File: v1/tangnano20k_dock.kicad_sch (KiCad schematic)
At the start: 42 parts, among them J1 Mini-DIN-6, J2 2x20 Pin Female, J3 Conn_01x03_Male, J4 Conn_01x20, J5 Conn_01x02, J6 RCA, J7 FCR684205T, J8 AudioJack3, U1 TXS0104E, U2 TangNano20K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

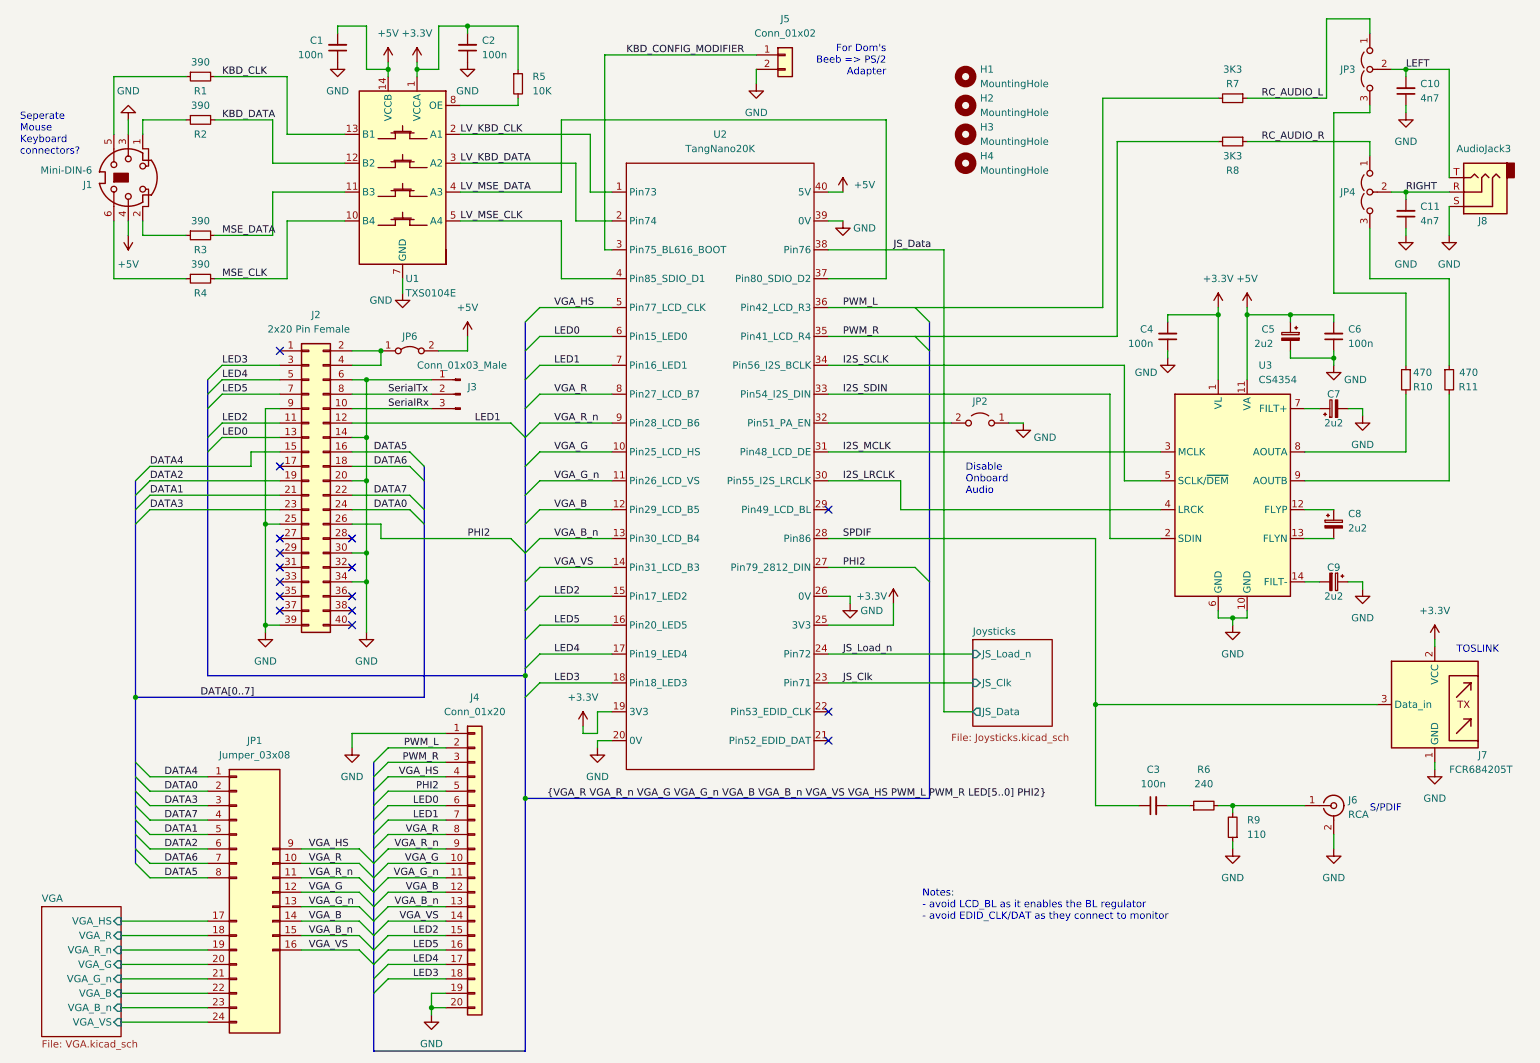
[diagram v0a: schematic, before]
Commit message: Add KEY_CONF to DEBUG header
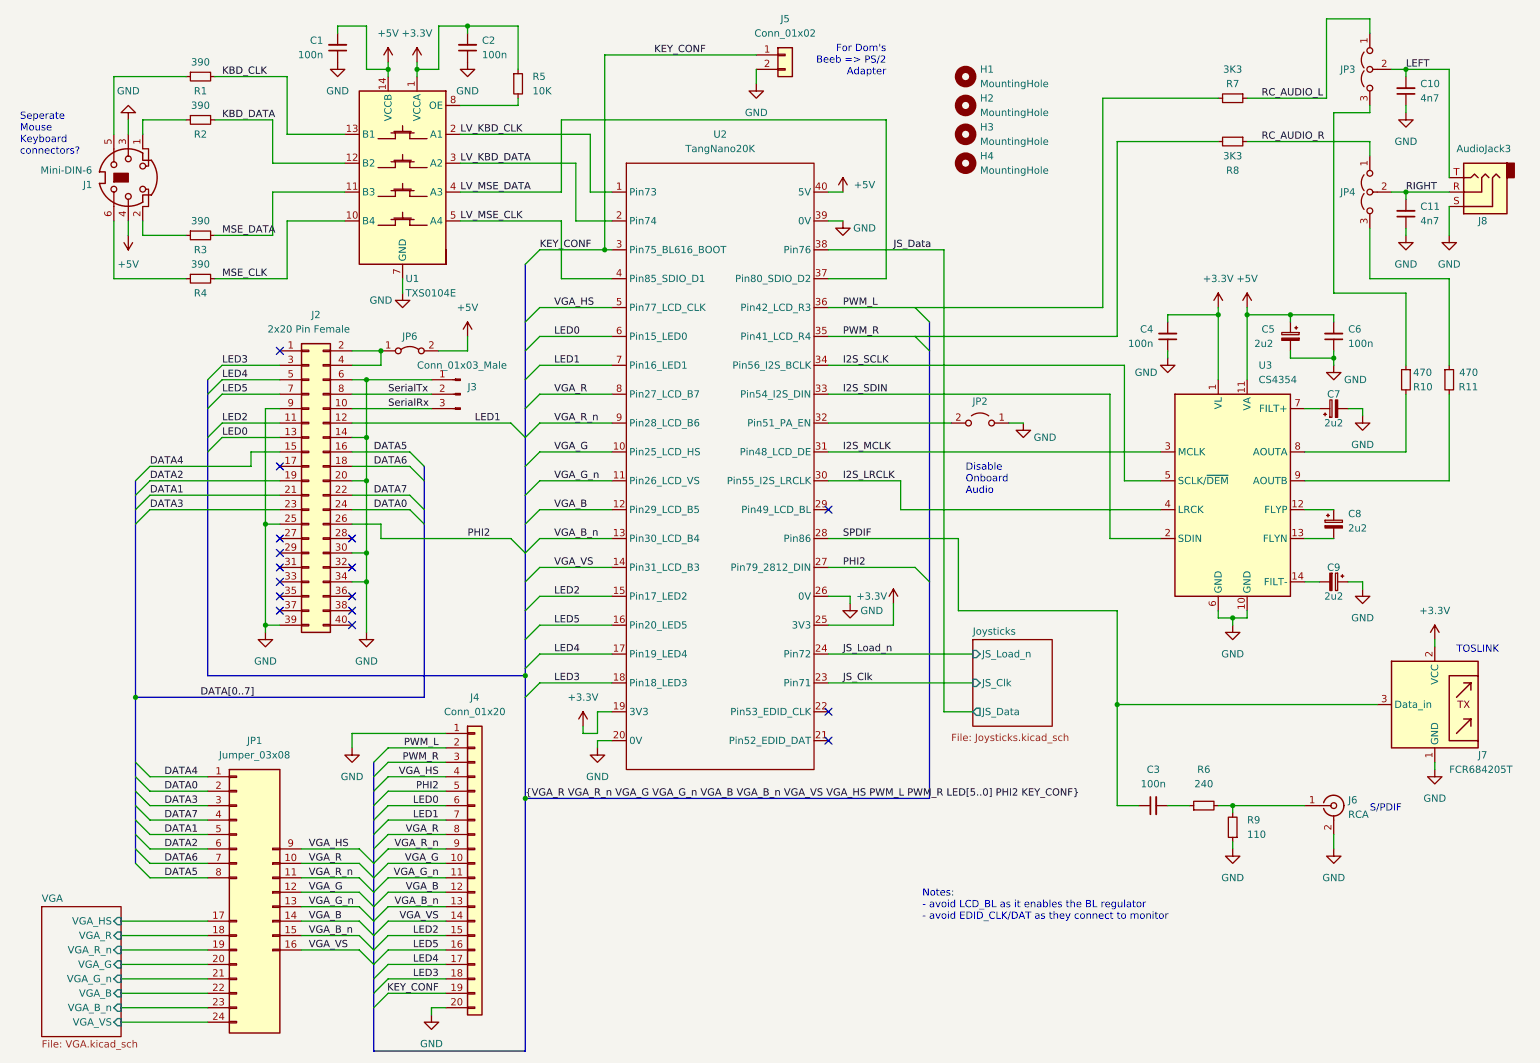
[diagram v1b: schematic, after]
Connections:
- net GND: no longer J4.19 (Pin_19)
- net KBD_CONFIG_MODIFIER renamed KEY_CONF
- net KEY_CONF: now also J4.19 (Pin_19)
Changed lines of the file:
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@@
   (junction (at 80.01 87.63) (diameter 0) (color 0 0 0 0)
   )
-  (junction (at 208.28 134.62) (diameter 0) (color 0 0 0 0)
-  )
   (junction (at 80.01 77.47) (diameter 0) (color 0 0 0 0)
   )
   (junction (at 62.23 102.87) (diameter 0) (color 0 0 0 0)
   )
-  (junction (at 91.44 187.96) (diameter 0) (color 0 0 0 0)
-  )
   (junction (at 39.37 133.35) (diameter 0) (color 0 0 0 0)
   )
@@
   (junction (at 62.23 120.65) (diameter 0) (color 0 0 0 0)
   )
+  (junction (at 212.09 134.62) (diameter 0) (color 0 0 0 0)
+  )
   (junction (at 82.55 72.39) (diameter 0) (color 0 0 0 0)
   )
@@
   (junction (at 242.57 66.04) (diameter 0) (color 0 0 0 0)
   )
+  (junction (at 121.92 54.61) (diameter 0) (color 0 0 0 0)
+  )
   (junction (at 80.01 95.25) (diameter 0) (color 0 0 0 0)
   )
@@
     (stroke (width 0) (type default) (color 0 0 0 0))
   )
+  (bus_entry (at 83.82 185.42) (size -2.54 2.54)
+    (stroke (width 0) (type default) (color 0 0 0 0))
+  )
   (bus_entry (at 41.91 154.94) (size -2.54 -2.54)
     (stroke (width 0) (type default) (color 0 0 0 0))
@@
     (stroke (width 0) (type default) (color 0 0 0 0))
   )
+  (bus_entry (at 110.49 54.61) (size -2.54 2.54)
+    (stroke (width 0) (type default) (color 0 0 0 0))
+  )
   (bus_entry (at 54.61 85.09) (size -2.54 2.54)
     (stroke (width 0) (type default) (color 0 0 0 0))
@@
     (stroke (width 0) (type default) (color 0 0 0 0))
   )
+  (wire (pts (xy 110.49 54.61) (xy 121.92 54.61))
+    (stroke (width 0) (type default) (color 0 0 0 0))
+  )
   (wire (pts (xy 212.09 35.56) (xy 229.87 35.56))
     (stroke (width 0) (type default) (color 0 0 0 0))
@@
     (stroke (width 0) (type default) (color 0 0 0 0))
   )
+  (wire (pts (xy 212.09 134.62) (xy 257.81 134.62))
+    (stroke (width 0) (type default) (color 0 0 0 0))
+  )
   (wire (pts (xy 40.64 31.75) (xy 48.26 31.75))
     (stroke (width 0) (type default) (color 0 0 0 0))
@@
     (stroke (width 0) (type default) (color 0 0 0 0))
   )
+  (wire (pts (xy 93.98 185.42) (xy 83.82 185.42))
+    (stroke (width 0) (type default) (color 0 0 0 0))
+  )
   (wire (pts (xy 53.34 59.69) (xy 66.04 59.69))
     (stroke (width 0) (type default) (color 0 0 0 0))
@@
     (stroke (width 0) (type default) (color 0 0 0 0))
   )
-  (wire (pts (xy 91.44 187.96) (xy 91.44 185.42))
-    (stroke (width 0) (type default) (color 0 0 0 0))
-  )
   (bus (pts (xy 81.28 144.78) (xy 81.28 147.32))
     (stroke (width 0) (type default) (color 0 0 0 0))
@@
     (stroke (width 0) (type default) (color 0 0 0 0))
   )
+  (wire (pts (xy 212.09 118.11) (xy 212.09 134.62))
+    (stroke (width 0) (type default) (color 0 0 0 0))
+  )
   (bus (pts (xy 107.95 77.47) (xy 107.95 82.55))
     (stroke (width 0) (type default) (color 0 0 0 0))
@@
     (stroke (width 0) (type default) (color 0 0 0 0))
   )
-  (wire (pts (xy 161.29 105.41) (xy 208.28 105.41))
+  (wire (pts (xy 161.29 105.41) (xy 184.15 105.41))
     (stroke (width 0) (type default) (color 0 0 0 0))
   )
@@
     (stroke (width 0) (type default) (color 0 0 0 0))
   )
-  (wire (pts (xy 208.28 134.62) (xy 257.81 134.62))
-    (stroke (width 0) (type default) (color 0 0 0 0))
-  )
   (wire (pts (xy 110.49 74.93) (xy 123.19 74.93))
     (stroke (width 0) (type default) (color 0 0 0 0))
@@
     (stroke (width 0) (type default) (color 0 0 0 0))
   )
-  (wire (pts (xy 208.28 105.41) (xy 208.28 134.62))
-    (stroke (width 0) (type default) (color 0 0 0 0))
-  )
   (wire (pts (xy 106.68 29.21) (xy 106.68 27.94))
     (stroke (width 0) (type default) (color 0 0 0 0))
@@
     (stroke (width 0) (type default) (color 0 0 0 0))
   )
-  (wire (pts (xy 208.28 152.4) (xy 215.9 152.4))
+  (wire (pts (xy 212.09 152.4) (xy 215.9 152.4))
     (stroke (width 0) (type default) (color 0 0 0 0))
   )
@@
     (stroke (width 0) (type default) (color 0 0 0 0))
   )
+  (wire (pts (xy 184.15 118.11) (xy 212.09 118.11))
+    (stroke (width 0) (type default) (color 0 0 0 0))
+  )
   (wire (pts (xy 232.41 158.75) (xy 232.41 160.02))
     (stroke (width 0) (type default) (color 0 0 0 0))
@@
     (stroke (width 0) (type default) (color 0 0 0 0))
   )
+  (wire (pts (xy 184.15 105.41) (xy 184.15 118.11))
+    (stroke (width 0) (type default) (color 0 0 0 0))
+  )
   (bus (pts (xy 107.95 133.35) (xy 107.95 151.13))
     (stroke (width 0) (type default) (color 0 0 0 0))
@@
     (stroke (width 0) (type default) (color 0 0 0 0))
   )
-  (wire (pts (xy 208.28 134.62) (xy 208.28 152.4))
+  (wire (pts (xy 212.09 134.62) (xy 212.09 152.4))
     (stroke (width 0) (type default) (color 0 0 0 0))
   )
@@
     (stroke (width 0) (type default) (color 0 0 0 0))
   )
-  (wire (pts (xy 91.44 185.42) (xy 93.98 185.42))
-    (stroke (width 0) (type default) (color 0 0 0 0))
-  )
   (wire (pts (xy 36.83 172.72) (xy 52.07 172.72))
     (stroke (width 0) (type default) (color 0 0 0 0))
@@
     (stroke (width 0) (type default) (color 0 0 0 0))
   )
-  (bus (pts (xy 81.28 185.42) (xy 81.28 195.58))
+  (bus (pts (xy 81.28 185.42) (xy 81.28 187.96))
     (stroke (width 0) (type default) (color 0 0 0 0))
   )
@@
     (stroke (width 0) (type default) (color 0 0 0 0))
   )
+  (bus (pts (xy 81.28 187.96) (xy 81.28 195.58))
+    (stroke (width 0) (type default) (color 0 0 0 0))
+  )
   (wire (pts (xy 62.23 82.55) (xy 62.23 102.87))
     (stroke (width 0) (type default) (color 0 0 0 0))
@@
     (stroke (width 0) (type default) (color 0 0 0 0))
   )
+  (bus (pts (xy 107.95 57.15) (xy 107.95 67.31))
+    (stroke (width 0) (type default) (color 0 0 0 0))
+  )
   (wire (pts (xy 68.58 175.26) (xy 78.74 175.26))
     (stroke (width 0) (type default) (color 0 0 0 0))
@@
     (effects (font (size 1.27 1.27)) (justify right bottom))
   )
-  (label "{VGA_R VGA_R_n VGA_G VGA_G_n VGA_B VGA_B_n VGA_VS VGA_HS PWM_L PWM_R LED[5..0] PHI2}"
-    (at 111.76 151.13 0)
+  (label "{VGA_R VGA_R_n VGA_G VGA_G_n VGA_B VGA_B_n VGA_VS VGA_HS PWM_L PWM_R LED[5..0] PHI2 KEY_CONF}"
+    (at 107.95 151.13 0)
     (effects (font (size 1.27 1.27)) (justify left bottom))
   )
@@
     (effects (font (size 1.27 1.27)) (justify left bottom))
   )
+  (label "KEY_CONF" (at 92.71 185.42 180)
+    (effects (font (size 1.27 1.27)) (justify right bottom))
+  )
   (label "RC_AUDIO_R" (at 237.49 35.56 0)
     (effects (font (size 1.27 1.27)) (justify left bottom))
@@
     (effects (font (size 1.27 1.27)) (justify right bottom))
   )
-  (label "KBD_CONFIG_MODIFIER" (at 125.73 20.32 0)
-    (effects (font (size 1.27 1.27)) (justify left bottom))
+  (label "KEY_CONF" (at 139.7 20.32 180)
+    (effects (font (size 1.27 1.27)) (justify right bottom))
   )
   (label "PHI2" (at 97.79 105.41 0)
@@
     (effects (font (size 1.27 1.27)) (justify right bottom))
   )
+  (label "KEY_CONF" (at 110.49 54.61 0)
+    (effects (font (size 1.27 1.27)) (justify left bottom))
+  )
   (label "DATA[0..7]" (at 50.8 133.35 0)

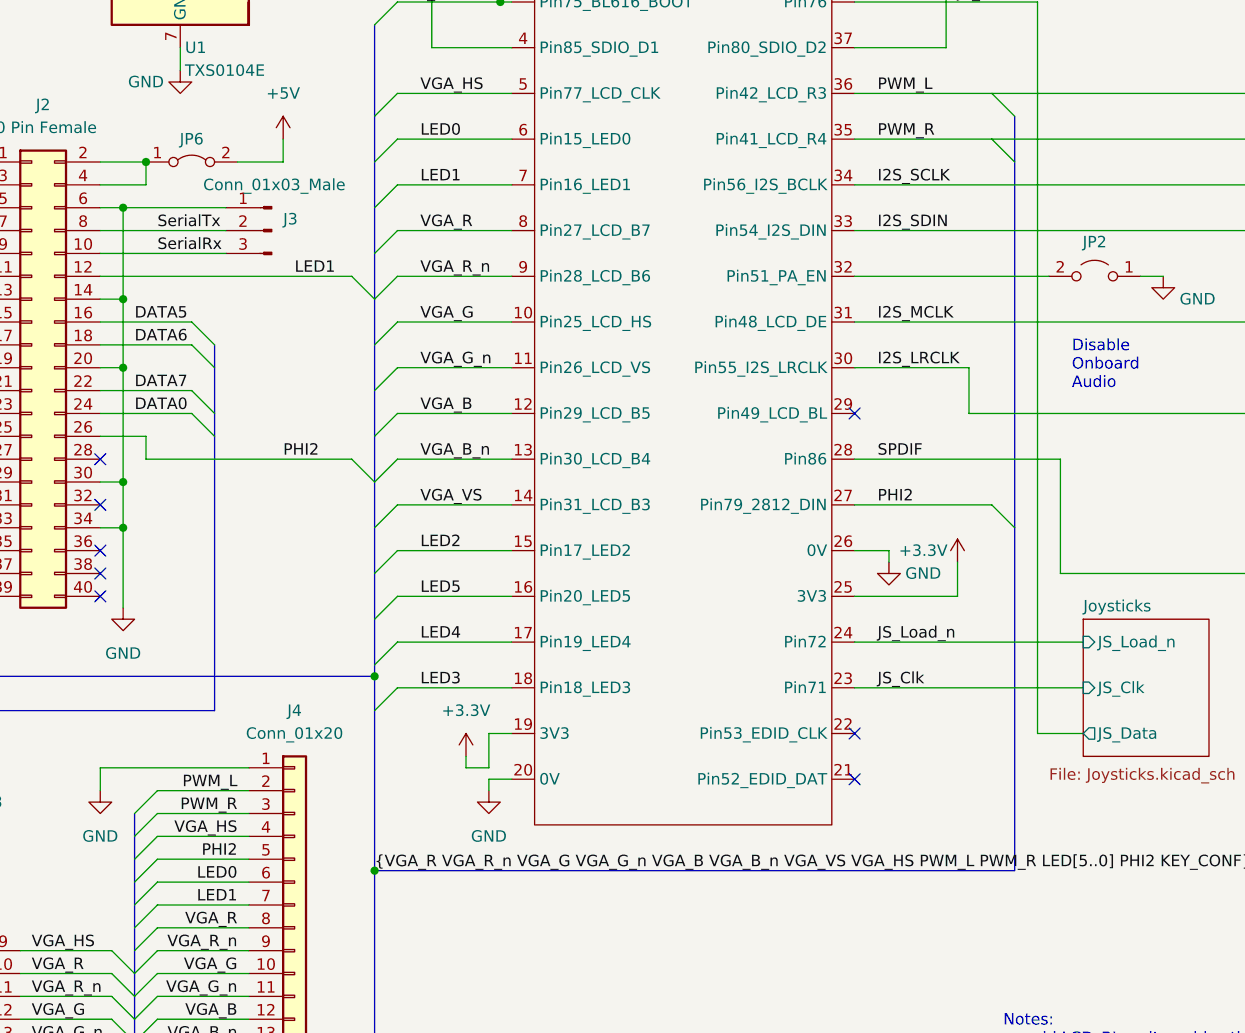
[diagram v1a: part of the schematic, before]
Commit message: Drive PiTube PHI2 from js_clk to save a pin
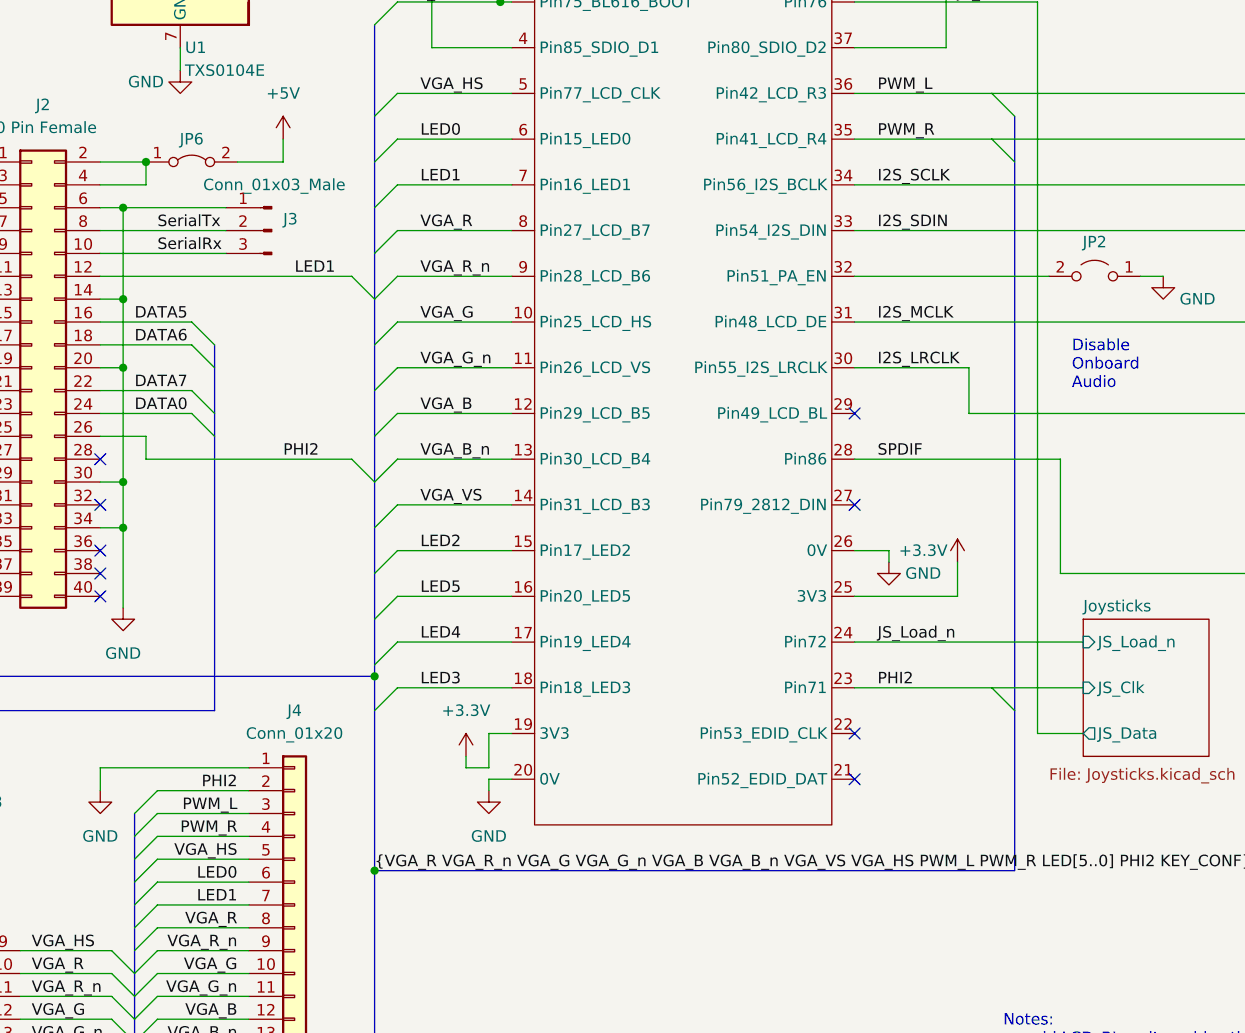
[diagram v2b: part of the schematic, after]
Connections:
- net JS_Clk is gone; now on net PHI2: U2.23 (Pin71)
- net PHI2: now also J4.2 (Pin_2); no longer J4.5 (Pin_5), U2.27 (Pin79_2812_DIN)
- net PWM_L: now also J4.3 (Pin_3); no longer J4.2 (Pin_2)
- net PWM_R: now also J4.4 (Pin_4); no longer J4.3 (Pin_3)
- net VGA_HS: now also J4.5 (Pin_5); no longer J4.4 (Pin_4)
- no-connect marks 16 -> 17
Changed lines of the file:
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@@
   (no_connect (at 64.77 107.95))
   (no_connect (at 64.77 72.39))
+  (no_connect (at 161.29 110.49))
   (no_connect (at 161.29 135.89))
   (no_connect (at 161.29 100.33))
@@
     (stroke (width 0) (type default) (color 0 0 0 0))
   )
-  (bus_entry (at 176.53 110.49) (size 2.54 2.54)
+  (bus_entry (at 176.53 130.81) (size 2.54 2.54)
     (stroke (width 0) (type default) (color 0 0 0 0))
   )
@@
     (stroke (width 0) (type default) (color 0 0 0 0))
   )
-  (bus (pts (xy 179.07 72.39) (xy 179.07 113.03))
-    (stroke (width 0) (type default) (color 0 0 0 0))
-  )
   (wire (pts (xy 74.93 15.24) (xy 80.01 15.24))
     (stroke (width 0) (type default) (color 0 0 0 0))
@@
     (stroke (width 0) (type default) (color 0 0 0 0))
   )
-  (wire (pts (xy 161.29 110.49) (xy 176.53 110.49))
-    (stroke (width 0) (type default) (color 0 0 0 0))
-  )
   (wire (pts (xy 36.83 185.42) (xy 52.07 185.42))
     (stroke (width 0) (type default) (color 0 0 0 0))
@@
     (stroke (width 0) (type default) (color 0 0 0 0))
   )
+  (bus (pts (xy 179.07 133.35) (xy 179.07 151.13))
+    (stroke (width 0) (type default) (color 0 0 0 0))
+  )
   (bus (pts (xy 81.28 157.48) (xy 81.28 160.02))
     (stroke (width 0) (type default) (color 0 0 0 0))
@@
     (stroke (width 0) (type default) (color 0 0 0 0))
   )
-  (wire (pts (xy 161.29 130.81) (xy 186.69 130.81))
+  (wire (pts (xy 161.29 130.81) (xy 176.53 130.81))
     (stroke (width 0) (type default) (color 0 0 0 0))
   )
@@
     (stroke (width 0) (type default) (color 0 0 0 0))
   )
+  (wire (pts (xy 176.53 130.81) (xy 186.69 130.81))
+    (stroke (width 0) (type default) (color 0 0 0 0))
+  )
   (bus (pts (xy 107.95 87.63) (xy 107.95 92.71))
     (stroke (width 0) (type default) (color 0 0 0 0))
@@
     (stroke (width 0) (type default) (color 0 0 0 0))
   )
-  (bus (pts (xy 179.07 113.03) (xy 179.07 151.13))
+  (bus (pts (xy 179.07 72.39) (xy 179.07 133.35))
     (stroke (width 0) (type default) (color 0 0 0 0))
   )
@@
     (effects (font (size 1.27 1.27)) (justify left bottom))
   )
-  (label "PWM_R" (at 92.71 144.78 180)
+  (label "PWM_R" (at 92.71 147.32 180)
     (effects (font (size 1.27 1.27)) (justify right bottom))
   )
@@
     (effects (font (size 1.27 1.27)) (justify left bottom))
   )
-  (label "VGA_HS" (at 92.71 147.32 180)
+  (label "VGA_HS" (at 92.71 149.86 180)
     (effects (font (size 1.27 1.27)) (justify right bottom))
   )
@@
     (effects (font (size 1.27 1.27)) (justify left bottom))
   )
-  (label "PHI2" (at 92.71 149.86 180)
+  (label "PHI2" (at 92.71 142.24 180)
     (effects (font (size 1.27 1.27)) (justify right bottom))
   )
@@
     (effects (font (size 1.27 1.27)) (justify left bottom))
   )
-  (label "PHI2" (at 163.83 110.49 0)
-    (effects (font (size 1.27 1.27)) (justify left bottom))
-  )
   (label "LED0" (at 54.61 87.63 0)
     (effects (font (size 1.27 1.27)) (justify left bottom))
@@
     (effects (font (size 1.27 1.27)) (justify left bottom))
   )
-  (label "PWM_L" (at 92.71 142.24 180)
+  (label "PWM_L" (at 92.71 144.78 180)
     (effects (font (size 1.27 1.27)) (justify right bottom))
   )
@@
     (effects (font (size 1.27 1.27)) (justify left bottom))
   )
-  (label "JS_Clk" (at 163.83 130.81 0)
+  (label "PHI2" (at 163.83 130.81 0)
     (effects (font (size 1.27 1.27)) (justify left bottom))
   )
